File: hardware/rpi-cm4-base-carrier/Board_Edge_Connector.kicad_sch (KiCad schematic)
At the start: 3 parts, among them J10 Conn_02x10_Odd_Even, J9 ERM8-040-01-X-D-EM2-L-XX, U9 74LVC1G07SE-7

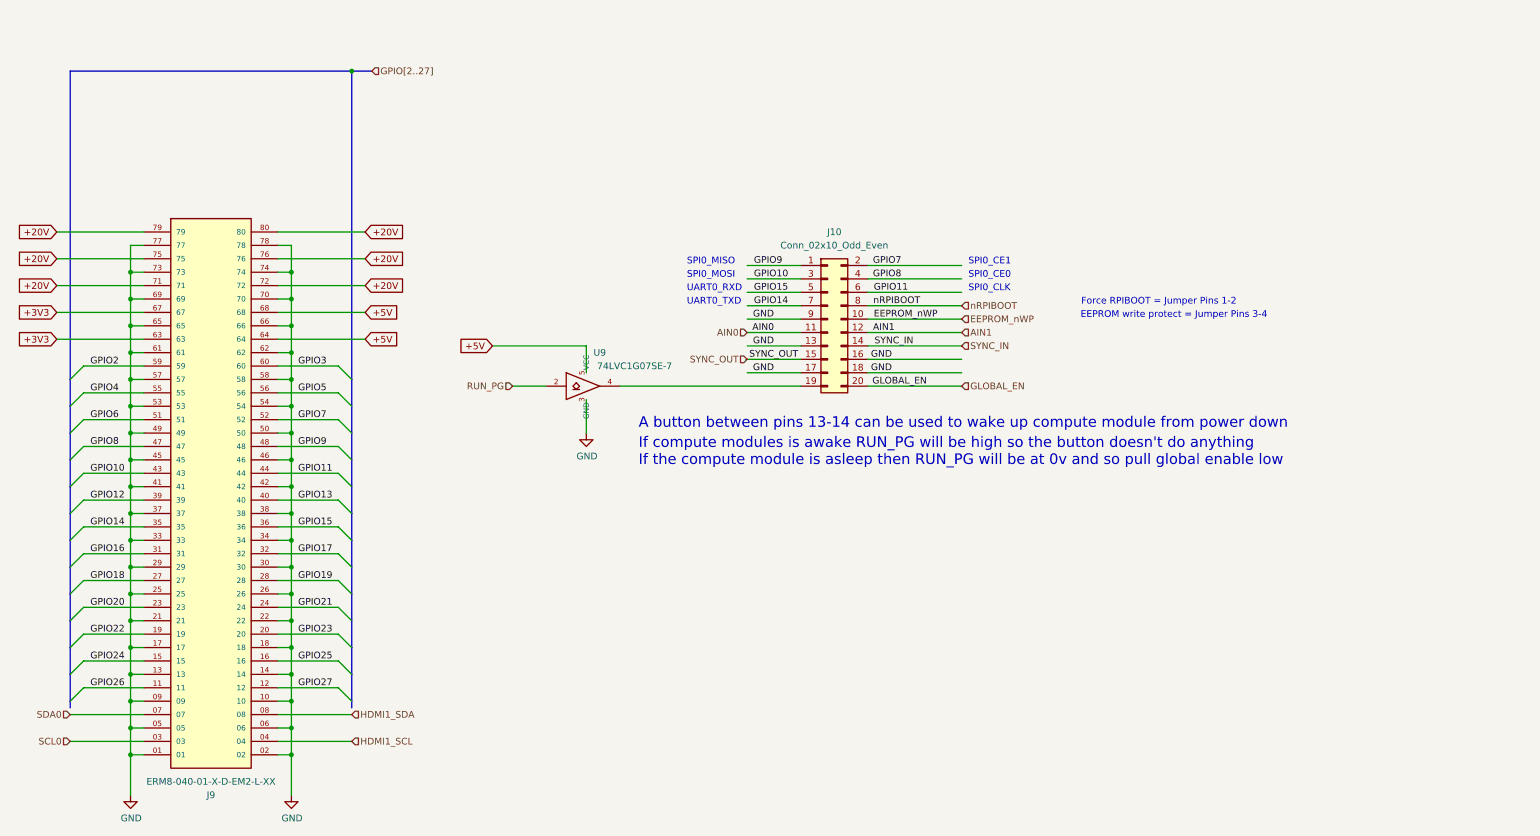
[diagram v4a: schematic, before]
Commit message: files updated to kicad 8, 2x10 connector updated to correct origin
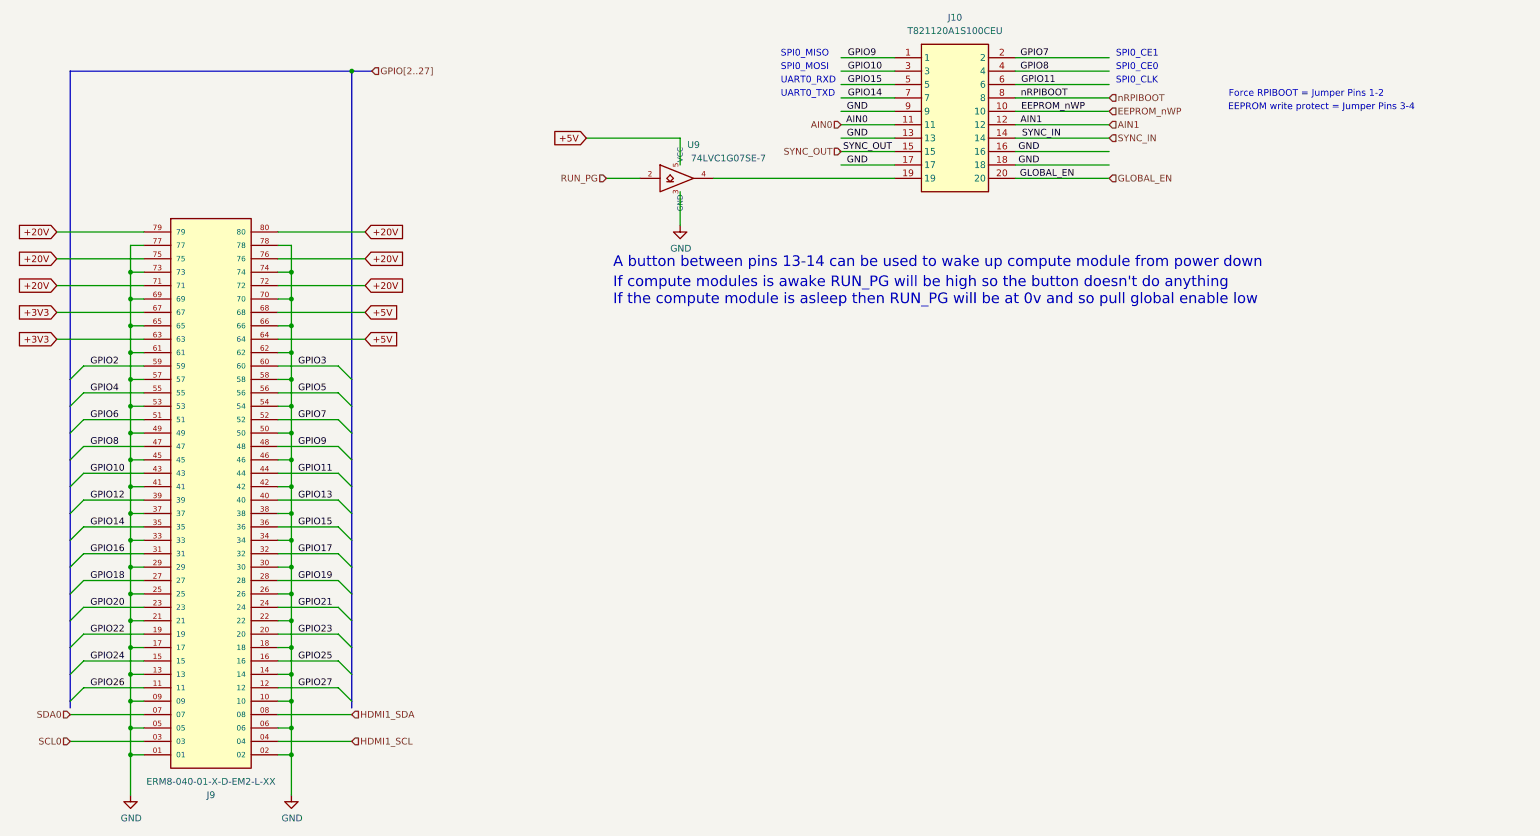
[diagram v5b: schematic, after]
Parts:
- removed J10: Conn_02x10_Odd_Even, Connector_IDC:IDC-Header_2x10_P2.54mm_Vertical, symbol Connector_Generic:Conn_02x10_Odd_Even
- added J10: T821120A1S100CEU, SHDR20W64P254X254_2X10_3302X895X915P, symbol SamacSys_Parts:T821120A1S100CEU
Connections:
- net AIN0: now also J10.11
- net AIN1: now also J10.12
- net EEPROM_nWP: now also J10.10
- net GLOBAL_EN: now also J10.20
- net GND: now also J10.13, J10.16, J10.17, J10.18, J10.9
- net GPIO10: now also J10.3
- net GPIO11: now also J10.6
- net GPIO14: now also J10.7
- net GPIO15: now also J10.5
- net GPIO7: now also J10.2
- net GPIO8: now also J10.4
- net GPIO9: now also J10.1
- net SYNC_IN: now also J10.14
- net SYNC_OUT: now also J10.15
- net nRPIBOOT: now also J10.8
- net at U9.4: now also J10.19
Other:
- moved on the sheet: U9

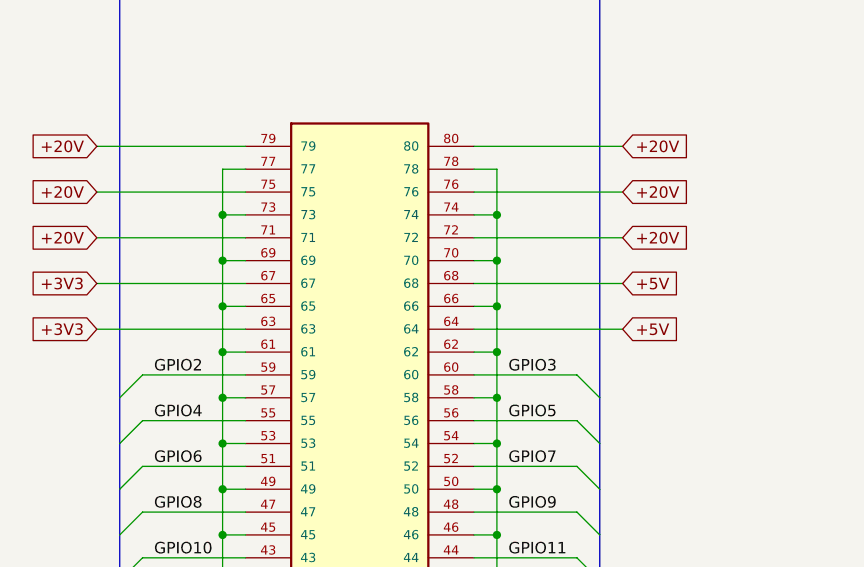
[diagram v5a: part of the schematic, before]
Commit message: moved edge samtec edge connector to correct positioning
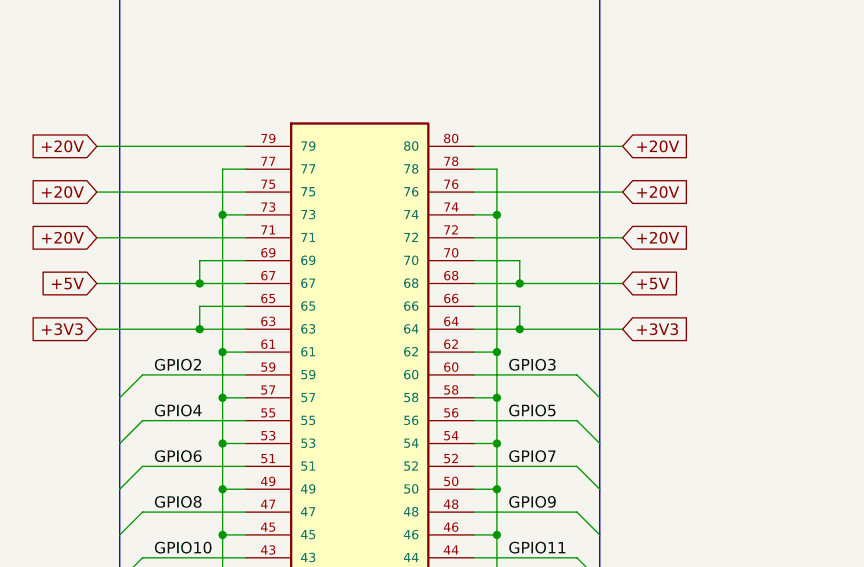
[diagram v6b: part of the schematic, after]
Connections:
- net +3V3: now also J9.64, J9.65, J9.66; no longer J9.67
- net +5V: now also J9.67, J9.69, J9.70; no longer J9.64
- net GND: no longer J9.65, J9.66, J9.69, J9.70
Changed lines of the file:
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@@
     (comment 4 "Author: Sam Earnshaw")
   )
+  (junction (at 69.85 77.47) (diameter 0) (color 0 0 0 0)
+  )
   (junction (at 67.31 140.97) (diameter 0) (color 0 0 0 0)
   )
-  (junction (at 36.83 80.01) (diameter 0) (color 0 0 0 0)
-  )
   (junction (at 36.83 105.41) (diameter 0) (color 0 0 0 0)
   )
@@
   (junction (at 36.83 69.85) (diameter 0) (color 0 0 0 0)
   )
+  (junction (at 34.29 77.47) (diameter 0) (color 0 0 0 0)
+  )
   (junction (at 36.83 100.33) (diameter 0) (color 0 0 0 0)
   )
@@
   (junction (at 36.83 85.09) (diameter 0) (color 0 0 0 0)
   )
+  (junction (at 34.29 82.55) (diameter 0) (color 0 0 0 0)
+  )
   (junction (at 36.83 135.89) (diameter 0) (color 0 0 0 0)
   )
@@
   (junction (at 67.31 156.21) (diameter 0) (color 0 0 0 0)
   )
-  (junction (at 67.31 74.93) (diameter 0) (color 0 0 0 0)
+  (junction (at 69.85 82.55) (diameter 0) (color 0 0 0 0)
   )
   (junction (at 36.83 110.49) (diameter 0) (color 0 0 0 0)
@@
   (junction (at 67.31 125.73) (diameter 0) (color 0 0 0 0)
   )
-  (junction (at 36.83 74.93) (diameter 0) (color 0 0 0 0)
-  )
   (junction (at 36.83 146.05) (diameter 0) (color 0 0 0 0)
   )
   (junction (at 78.74 31.75) (diameter 0) (color 0 0 0 0)
   )
-  (junction (at 67.31 80.01) (diameter 0) (color 0 0 0 0)
-  )
   (junction (at 67.31 110.49) (diameter 0) (color 0 0 0 0)
   )
@@
     (stroke (width 0) (type solid))
   )
+  (wire (pts (xy 69.85 77.47) (xy 81.28 77.47))
+    (stroke (width 0) (type default))
+  )
   (wire (pts (xy 36.83 90.17) (xy 39.37 90.17))
     (stroke (width 0) (type default))
@@
     (stroke (width 0) (type solid))
   )
+  (wire (pts (xy 64.77 80.01) (xy 69.85 80.01))
+    (stroke (width 0) (type default))
+  )
   (bus (pts (xy 25.4 105.41) (xy 25.4 100.33))
     (stroke (width 0) (type default))
@@
     (stroke (width 0) (type default))
   )
-  (wire (pts (xy 67.31 74.93) (xy 67.31 80.01))
+  (wire (pts (xy 34.29 82.55) (xy 39.37 82.55))
     (stroke (width 0) (type default))
   )
@@
     (stroke (width 0) (type default))
   )
-  (wire (pts (xy 67.31 80.01) (xy 67.31 85.09))
-    (stroke (width 0) (type default))
-  )
   (wire (pts (xy 27.94 97.79) (xy 39.37 97.79))
     (stroke (width 0) (type default))
@@
     (stroke (width 0) (type solid))
   )
-  (wire (pts (xy 36.83 74.93) (xy 39.37 74.93))
+  (wire (pts (xy 69.85 74.93) (xy 69.85 77.47))
     (stroke (width 0) (type default))
   )
@@
     (stroke (width 0) (type default))
   )
-  (wire (pts (xy 36.83 85.09) (xy 36.83 80.01))
-    (stroke (width 0) (type default))
-  )
   (wire (pts (xy 64.77 107.95) (xy 76.2 107.95))
     (stroke (width 0) (type default))
@@
     (stroke (width 0) (type default))
   )
-  (wire (pts (xy 64.77 77.47) (xy 81.28 77.47))
+  (wire (pts (xy 64.77 77.47) (xy 69.85 77.47))
+    (stroke (width 0) (type default))
+  )
+  (wire (pts (xy 34.29 77.47) (xy 39.37 77.47))
     (stroke (width 0) (type default))
   )
@@
     (stroke (width 0) (type default))
   )
-  (wire (pts (xy 64.77 74.93) (xy 67.31 74.93))
+  (wire (pts (xy 69.85 82.55) (xy 81.28 82.55))
     (stroke (width 0) (type default))
   )
@@
     (stroke (width 0) (type default))
   )
+  (wire (pts (xy 39.37 74.93) (xy 34.29 74.93))
+    (stroke (width 0) (type default))
+  )
   (wire (pts (xy 27.94 138.43) (xy 39.37 138.43))
     (stroke (width 0) (type default))
   )
+  (wire (pts (xy 34.29 80.01) (xy 34.29 82.55))
+    (stroke (width 0) (type default))
+  )
   (wire (pts (xy 67.31 161.29) (xy 67.31 156.21))
     (stroke (width 0) (type default))
   )
-  (wire (pts (xy 67.31 69.85) (xy 67.31 74.93))
+  (wire (pts (xy 67.31 69.85) (xy 67.31 85.09))
     (stroke (width 0) (type default))
   )
@@
     (stroke (width 0) (type default))
   )
+  (wire (pts (xy 64.77 74.93) (xy 69.85 74.93))
+    (stroke (width 0) (type default))
+  )
   (wire (pts (xy 36.83 146.05) (xy 39.37 146.05))
     (stroke (width 0) (type default))
@@
     (stroke (width 0) (type default))
   )
-  (wire (pts (xy 22.86 77.47) (xy 39.37 77.47))
+  (wire (pts (xy 22.86 77.47) (xy 34.29 77.47))
     (stroke (width 0) (type default))
   )
@@
     (stroke (width 0) (type default))
   )
+  (wire (pts (xy 69.85 80.01) (xy 69.85 82.55))
+    (stroke (width 0) (type default))
+  )
   (wire (pts (xy 36.83 64.77) (xy 39.37 64.77))
     (stroke (width 0) (type default))
@@
     (stroke (width 0) (type default))
   )
-  (wire (pts (xy 64.77 82.55) (xy 81.28 82.55))
+  (wire (pts (xy 39.37 80.01) (xy 34.29 80.01))
+    (stroke (width 0) (type default))
+  )
+  (wire (pts (xy 64.77 82.55) (xy 69.85 82.55))
     (stroke (width 0) (type default))
   )
@@
     (stroke (width 0) (type default))
   )
-  (wire (pts (xy 36.83 74.93) (xy 36.83 69.85))
-    (stroke (width 0) (type default))
-  )
   (wire (pts (xy 27.94 87.63) (xy 39.37 87.63))
     (stroke (width 0) (type default))
@@
     (stroke (width 0) (type default))
   )
+  (wire (pts (xy 34.29 74.93) (xy 34.29 77.47))
+    (stroke (width 0) (type default))
+  )
   (wire (pts (xy 27.94 133.35) (xy 39.37 133.35))
     (stroke (width 0) (type default))
@@
     (stroke (width 0) (type default))
   )
-  (wire (pts (xy 22.86 82.55) (xy 39.37 82.55))
+  (wire (pts (xy 22.86 82.55) (xy 34.29 82.55))
     (stroke (width 0) (type default))
   )
@@
     (stroke (width 0) (type default))
   )
-  (wire (pts (xy 36.83 80.01) (xy 36.83 74.93))
+  (wire (pts (xy 36.83 69.85) (xy 36.83 85.09))
     (stroke (width 0) (type default))
   )
@@
     (stroke (width 0) (type default))
   )
-  (wire (pts (xy 64.77 80.01) (xy 67.31 80.01))
-    (stroke (width 0) (type default))
-  )
   (wire (pts (xy 36.83 120.65) (xy 39.37 120.65))
     (stroke (width 0) (type default))
@@
   (wire (pts (xy 140.97 54.61) (xy 140.97 60.96))
     (stroke (width 0) (type solid))
-  )
-  (wire (pts (xy 36.83 80.01) (xy 39.37 80.01))
-    (stroke (width 0) (type default))
   )
   (wire (pts (xy 36.83 95.25) (xy 36.83 90.17))
@@
     )
   )
-  (global_label "+3V3" (shape input) (at 22.86 77.47 180) (fields_autoplaced)
+  (global_label "+5V" (shape input) (at 22.86 77.47 180) (fields_autoplaced)
     (effects (font (size 1.27 1.27)) (justify right))
-    (property "Intersheetrefs" "${INTERSHEET_REFS}" (at 14.6997 77.47 0)
+    (property "Intersheetrefs" "${INTERSHEET_REFS}" (at 15.9092 77.47 0)
       (effects (font (size 1.27 1.27)) (justify right) hide)
     )
@@
     )
   )
-  (global_label "+5V" (shape input) (at 81.28 82.55 0) (fields_autoplaced)
-    (effects (font (size 1.27 1.27)) (justify left))
-    (property "Intersheetrefs" "${INTERSHEET_REFS}" (at 88.2308 82.55 0)
-      (effects (font (size 1.27 1.27)) (justify left) hide)
-    )
-  )
   (global_label "+20V" (shape input) (at 22.86 72.39 180) (fields_autoplaced)
     (effects (font (size 1.27 1.27)) (justify right))
@@
       (effects (font (size 1.27 1.27)) (justify left) hide)
     )
+  )
+  (global_label "+3V3" (shape input) (at 81.28 82.55 0) (fields_autoplaced)
+    (effects (font (size 1.27 1.27)) (justify left))
+    (property "Intersheetrefs" "${INTERSHEET_REFS}" (at 89.4403 82.55 0)
+      (effects (font (size 1.27 1.27)) (justify left) hide)
+    )
